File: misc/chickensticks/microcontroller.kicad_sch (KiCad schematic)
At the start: 41 parts, among them J1 Conn_01x05_Pin, J2 HRO_TYPE-C-31-M-12, J3 Conn_01x04, J4 Conn_01x06, J5 Conn_01x06, J6 Conn_01x04, J7 Conn_01x04, Q3 2N7002, SW1 SKRPANE010, SW2 EC11E18244AU, U1 USBLC6-2SC6, U2 STM32L433CCTx, U3 TJA1042T-3, Y1 25 MHz

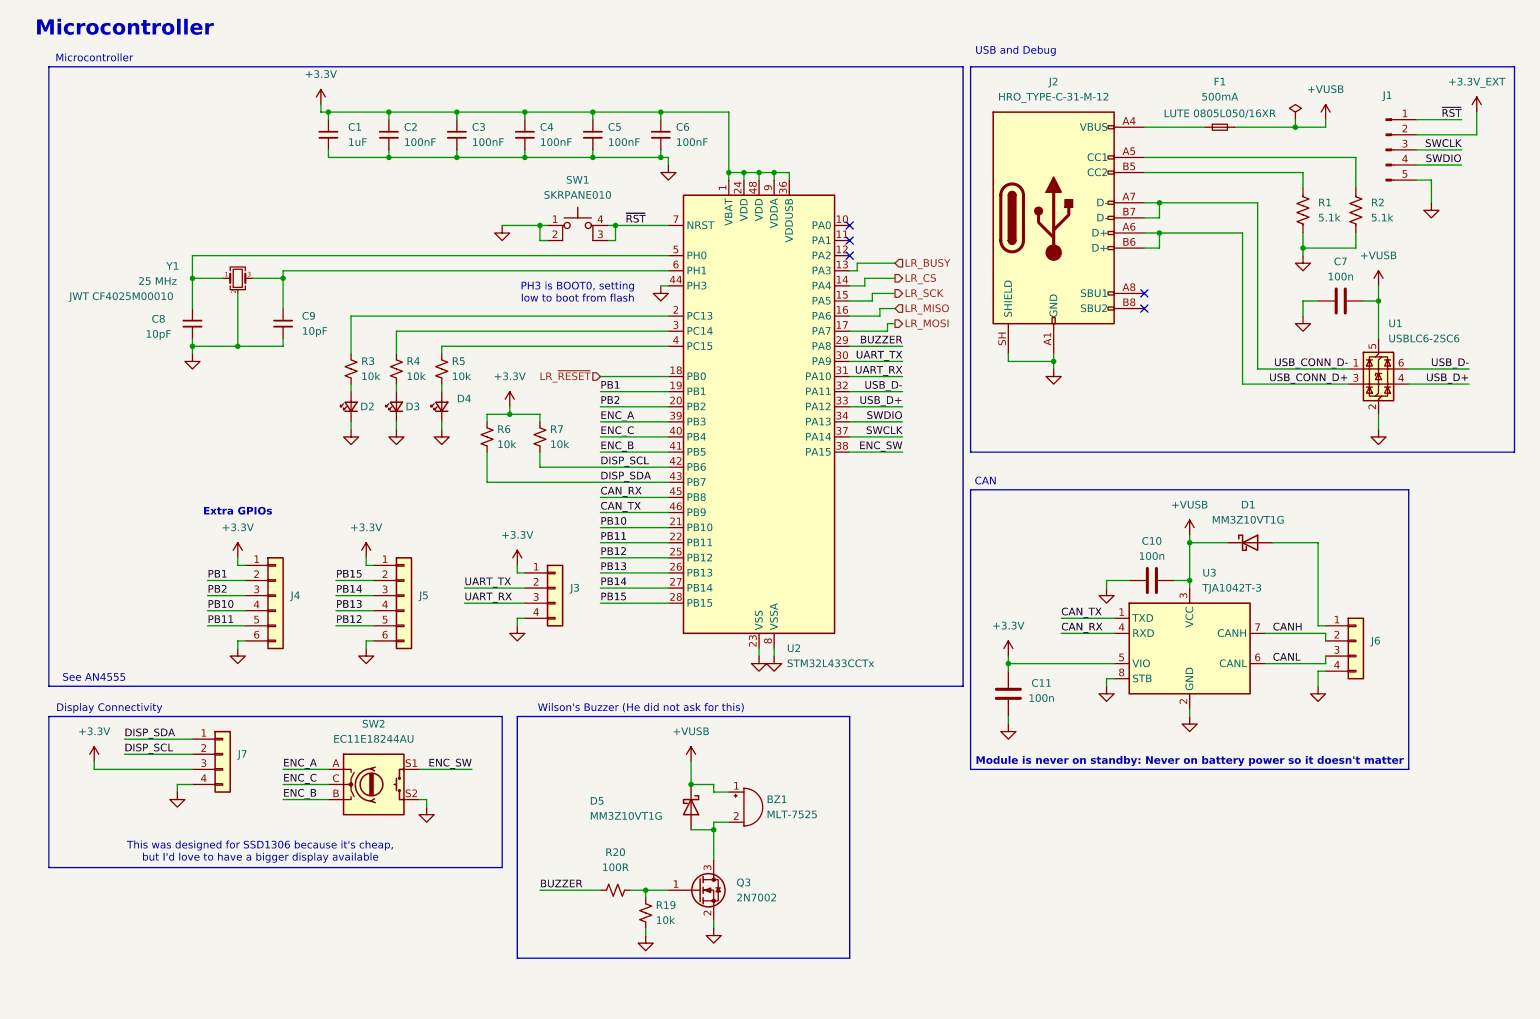
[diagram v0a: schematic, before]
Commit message: Simplify chickensticks, get isospi-tx ready, and update some cubemx projects
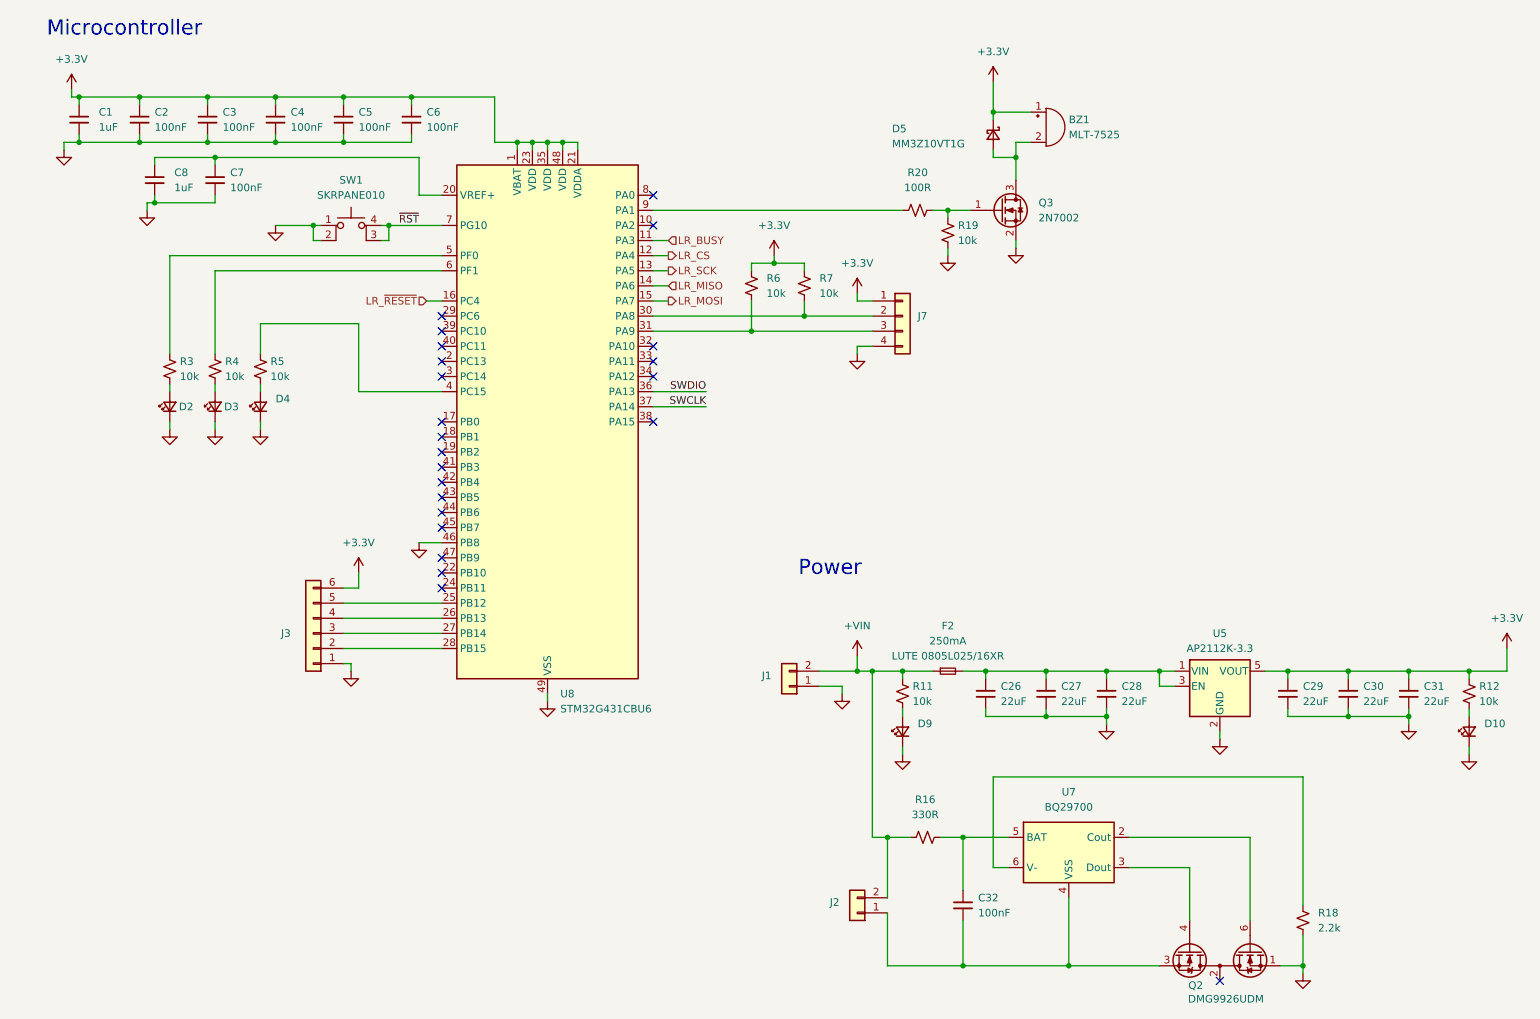
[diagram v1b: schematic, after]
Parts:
- removed C10, C11, C7: 100n, APRL_Passive:C_0603, symbol Device:C
- removed C9: 10pF, APRL_Passive:C_0603, symbol Device:C_Small
- removed D1: MM3Z10VT1G, APRL_Passive:SOD-323, symbol Diode:SS14
- removed F1: 500mA, APRL_Passive:Fuse_0805_2012Metric, symbol Device:Fuse_Small
- removed J1: Conn_01x05_Pin, Connector_PinHeader_2.54mm:PinHeader_1x05_P2.54mm_Vertical, symbol Connector:Conn_01x05_Pin
- removed J2: HRO_TYPE-C-31-M-12, APRL_Connector:USB_C_Receptacle_HRO_TYPE-C-31-M-12, symbol Connector:USB_C_Receptacle_USB2.0_16P
- removed J3, J6: Conn_01x04, Connector_PinHeader_2.54mm:PinHeader_1x04_P2.54mm_Vertical, symbol Connector_Generic:Conn_01x04
- removed J4, J5: Conn_01x06, Connector_PinHeader_2.54mm:PinHeader_1x06_P2.54mm_Vertical, symbol Connector_Generic:Conn_01x06
- removed R1, R2: 5.1k, APRL_Passive:R_0603, symbol Device:R_US
- removed SW2: EC11E18244AU, APRL_Module:RotaryEncoder_Alps_EC11E-Switch_Vertical_H20mm_MountingHoles, symbol APRL_Connector:RotaryEncoder_Switch
- removed U1: USBLC6-2SC6, Package_TO_SOT_SMD:SOT-23-6, symbol Power_Protection:USBLC6-2SC6
- removed U2: STM32L433CCTx, Package_QFP:LQFP-48_7x7mm_P0.5mm, symbol MCU_ST_STM32L4:STM32L433CCTx
- removed U3: TJA1042T-3, Package_SO:SOIC-8_3.9x4.9mm_P1.27mm, symbol Interface_CAN_LIN:TJA1042T-3
- removed Y1: 25 MHz, APRL_Passive:3225-4P-L, symbol Device:Crystal_GND24_Small
- added C26, C27, C28, C29, C30, C31: 22uF, APRL_Passive:C_0805, symbol Device:C_Small
- added C32, C7: 100nF, APRL_Passive:C_0603, symbol Device:C_Small
- added D10, D9: LED_Small, APRL_Passive:LED_0603, symbol Device:LED_Small
- added F2: 250mA, APRL_Passive:Fuse_0805_2012Metric, symbol Device:Fuse_Small
- added J1, J2: Conn_01x02, Connector_Molex:Molex_KK-254_AE-6410-02A_1x02_P2.54mm_Vertical, symbol Connector_Generic:Conn_01x02
- added J3: Conn_01x06, Connector_Molex:Molex_KK-254_AE-6410-06A_1x06_P2.54mm_Vertical, symbol Connector_Generic:Conn_01x06
- added Q2: DMG9926UDM, Package_TO_SOT_SMD:SOT-23-6, symbol Transistor_FET:DMG9926UDM
- added R11, R12: 10k, APRL_Passive:R_0603, symbol Device:R_Small_US
- added R16: 330R, APRL_Passive:R_0603, symbol Device:R_Small_US
- added R18: 2.2k, APRL_Passive:R_0603, symbol Device:R_Small_US
- added U5: AP2112K-3.3, Package_TO_SOT_SMD:SOT-23-5, symbol Regulator_Linear:AP2112K-3.3
- added U7: BQ29700, Package_SON:WSON-6_1.5x1.5mm_P0.5mm, symbol Battery_Management:BQ297xy
- added U8: STM32G431CBU6, APRL_Package_QFN:QFN-48_EP_7.3x7.3_Pitch0.5mm, symbol MCU_ST_STM32G4:STM32G431CBUx
- C8: value 10pF -> 1uF; footprint APRL_Passive:C_0603 -> APRL_Passive:C_0805
- D5: symbol Diode:SS14 -> Device:D_Schottky_Small
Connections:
- net +VUSB is gone; now on net +3.3V: BZ1.1 (+), D5.1 (K)
- net +3.3V: now also J7.1 (Pin_1), C29.1, C30.1, C31.1, J3.6 (Pin_6), R12.1, U5.5 (VOUT), U8.1 (VBAT), U8.21 (VDDA), U8.23 (VDD), U8.35 (VDD), U8.48 (VDD); no longer J7.3 (Pin_3)
- net GND: now also C26.2, C27.2, C28.2, C29.2, C30.2, C31.2, C7.2, D10.1 (K), D9.1 (K), J1.1 (Pin_1), J3.1 (Pin_1), Q2.1 (D1), R18.2, U5.2 (GND), U8.46 (PB8), U8.49 (VSS)
- net LR_BUSY: now also U8.11 (PA3)
- net LR_CS: now also U8.12 (PA4)
- net LR_MISO: now also U8.14 (PA6)
- net LR_MOSI: now also U8.15 (PA7)
- net LR_SCK: now also U8.13 (PA5)
- net LR_~{RESET}: now also U8.16 (PC4)
- net SWCLK: now also U8.37 (PA14)
- net SWDIO: now also U8.36 (PA13)
- net ~{RST}: now also U8.7 (PG10)
- net at C8.1: now also C7.1, U8.20 (VREF+)
- net at R3.1: now also U8.5 (PF0)
- net at R4.1: now also U8.6 (PF1)
- net at R5.1: now also U8.4 (PC15)
- net BUZZER: no longer names the net of R20.1
- net BUZZER: now also U8.9 (PA1)
- net DISP_SCL: no longer names the net of J7.2 (Pin_2), R7.2
- net DISP_SCL: now also U8.30 (PA8)
- net DISP_SDA: no longer names the net of R6.2
- net DISP_SDA: now also J7.3 (Pin_3), U8.31 (PA9); no longer J7.1 (Pin_1)
- new net: J3.2 (Pin_2), U8.28 (PB15)
- new net: J3.3 (Pin_3), U8.27 (PB14)
- new net: J3.4 (Pin_4), U8.26 (PB13)
- new net: J3.5 (Pin_5), U8.25 (PB12)
- new net: D10.2 (A), R12.2
- new net: D9.2 (A), R11.2
- new net: C26.1, C27.1, C28.1, F2.2, U5.1 (VIN), U5.3 (EN)
- new net: R18.1, U7.6 (V-)
- new net: C32.1, R16.2, U7.5 (BAT)
- new net: C32.2, J2.1 (Pin_1), Q2.3 (S2), U7.4 (VSS)
- new net: Q2.6 (G1), U7.2 (Cout)
- new net: Q2.4 (G2), U7.3 (Dout)
- new net: Q2.2 (S1/D2), Q2.5 (S1/D2)
- new net +VIN: F2.1, J1.2 (Pin_2), J2.2 (Pin_2), R11.1, R16.1
- no-connect marks 5 -> 23
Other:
- note added: "Power"
- note removed: "CAN"
- note removed: "Display Connectivity"
- note removed: "Extra GPIOs"
- note removed: "Module is never on standby: Never on battery power so it doesn't matter"
- note removed: "PH3 is BOOT0, setting low to boot from flash"
- note removed: "See AN4555"
- note removed: "This was designed for SSD1306 because it's cheap, but I'd love to have a bigger display available"
- note removed: "USB and Debug"
- note removed: "Wilson's Buzzer (He did not ask for this)"
- company: Aggie Propulsion & Rocketry Lab -> (none)
- title: Chickenstick -> (none)
- moved on the sheet: BZ1, C1, C2, C3, C4, C5, C6, D2, D3, D4, D5, Q3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

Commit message: Remove gps, add debug connector to chickensticks, and update rules for isospi and cs
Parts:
- added J10: Conn_01x04, Connector_PinHeader_2.54mm:PinHeader_1x04_P2.54mm_Vertical, symbol Connector_Generic:Conn_01x04
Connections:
- net +3.3V: now also J10.1 (Pin_1)
- net GND: now also J10.4 (Pin_4)
- net SWCLK: no longer names the net of U8.37 (PA14)
- net SWCLK: now also J10.3 (Pin_3)
- net SWDIO: no longer names the net of U8.36 (PA13)
- net SWDIO: now also J10.2 (Pin_2)
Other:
- moved on the sheet: C26, C27, C28, C29, C30, C31, C32, D10, D9, F2, J1, J2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
